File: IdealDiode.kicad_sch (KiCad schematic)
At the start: 11 parts, among them J1 Conn_01x01_Pin, J2 Conn_01x01_Pin, J3 Conn_01x01_Pin, J4 Conn_01x01_Pin, Q1 AO3400A, Q2 AO3401A, U1 LM393

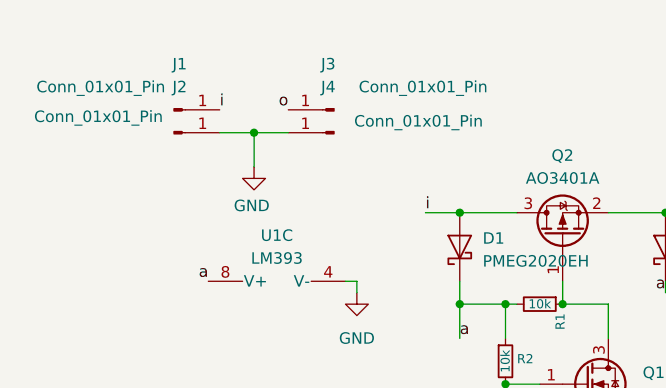
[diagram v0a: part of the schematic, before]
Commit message: Fixed wrong footprint issue
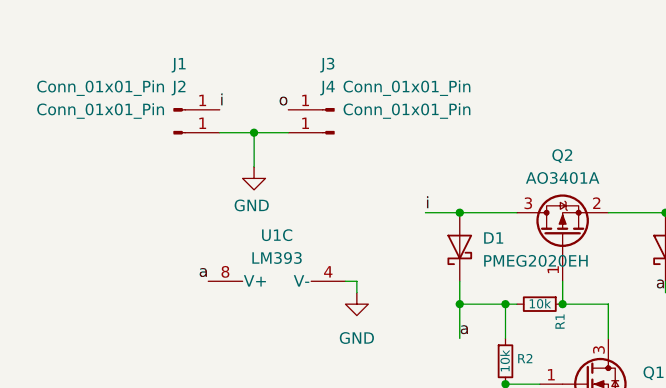
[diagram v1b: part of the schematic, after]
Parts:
- J1, J2, J3, J4: footprint Connector_PinSocket_2.54mm:PinSocket_1x01_P2.54mm_Vertical -> Connector_PinHeader_2.54mm:PinHeader_1x01_P2.54mm_Vertical

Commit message: Modified the design to be single-sided, prepared for PCBA at JLCPCB
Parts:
- D1, D2: LCSC Part # (none) -> C52287409
- J1, J2, J3, J4: now not fitted
- Q1: LCSC Part # (none) -> C20917
- Q2: LCSC Part # (none) -> C15127
- R1, R2: LCSC Part # (none) -> C25531
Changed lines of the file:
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@@
+			)
+		)
+		(property "LCSC Part #" "C25531"
+			(at 90.17 133.35 0)
+			(hide yes)
+			(show_name no)
+			(do_not_autoplace no)
+			(effects
+				(font
+					(size 1.27 1.27)
+				)
 			)
 		)
@@
 		(on_board yes)
 		(in_pos_files yes)
-		(dnp no)
+		(dnp yes)
 		(property "Reference" "J2"
 			(at 50.165 109.22 0)
@@
 		)
 		(property "Description" "30V Vds, 5.7A Id, N-Channel MOSFET, SOT-23"
+			(at 95.25 142.24 0)
+			(hide yes)
+			(show_name no)
+			(do_not_autoplace no)
+			(effects
+				(font
+					(size 1.27 1.27)
+				)
+			)
+		)
+		(property "LCSC Part #" "C20917"
 			(at 95.25 142.24 0)
 			(hide yes)
@@
 			)
 		)
+		(property "LCSC Part #" "C52287409"
+			(at 104.14 127 90)
+			(hide yes)
+			(show_name no)
+			(do_not_autoplace no)
+			(effects
+				(font
+					(size 1.27 1.27)
+				)
+			)
+		)
 		(pin "1"
 		)
@@
 		(on_board yes)
 		(in_pos_files yes)
-		(dnp no)
+		(dnp yes)
 		(property "Reference" "J4"
 			(at 66.675 109.22 0)
@@
 			)
 		)
+		(property "LCSC Part #" "C15127"
+			(at 92.71 125.73 90)
+			(hide yes)
+			(show_name no)
+			(do_not_autoplace no)
+			(effects
+				(font
+					(size 1.27 1.27)
+				)
+			)
+		)
 		(pin "3"
 		)
@@
 			)
 		)
+		(property "LCSC Part #" "C25531"
+			(at 86.36 139.7 0)
+			(hide yes)
+			(show_name no)
+			(do_not_autoplace no)
+			(effects
+				(font
+					(size 1.27 1.27)
+				)
+			)
+		)
 		(pin "2"
 		)
@@
 			)
 		)
+		(property "LCSC Part #" "C52287409"
+			(at 81.28 127 90)
+			(hide yes)
+			(show_name no)
+			(do_not_autoplace no)
+			(effects
+				(font
+					(size 1.27 1.27)
+				)
+			)
+		)
 		(pin "1"
 		)
@@
 		(on_board yes)
 		(in_pos_files yes)
-		(dnp no)
+		(dnp yes)
 		(property "Reference" "J1"
 			(at 50.165 106.68 0)
@@
 		(on_board yes)
 		(in_pos_files yes)
-		(dnp no)
+		(dnp yes)
 		(property "Reference" "J3"
 			(at 66.675 106.68 0)
